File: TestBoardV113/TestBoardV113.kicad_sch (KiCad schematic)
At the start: 98 parts, among them J1 Conn_01x02_Socket, J10 Conn_01x02_Pin, J11 Conn_01x02_Pin, J12 Conn_01x02_Pin, J13 Conn_02x03_Odd_Even, J14 Conn_02x03_Odd_Even, J15 Conn_01x02_Pin, J16 Conn_02x03_Odd_Even, J17 Conn_01x01_Pin, J18 Conn_01x28_Socket, J19 Conn_01x01_Pin, J2 Conn_02x06_Odd_Even, J20 Conn_01x01_Pin, J21 Conn_01x28_Socket, J22 Conn_01x02_Pin, J23 Conn_01x02_Socket, J24 Conn_01x01_Pin, J25 Conn_01x02_Pin, J26 Conn_01x02_Pin, J27 Conn_02x03_Odd_Even, J28 Conn_01x02_Socket, J3 Conn_01x02_Pin, J4 Conn_01x02_Pin, J5 Conn_01x02_Pin, J6 Conn_01x02_Pin, J7 Conn_01x03_Pin, J8 Conn_01x03_Pin, J9 Conn_01x03_Pin, SW1 SW_DIP_x07, U1 NCP705MTADJTCG, U2 NCP705MTADJTCG, U3 NCP705MTADJTCG, U4 TAR5SxxU_SOT353F, U5 TXB0104PW, U6 TXB0104PW

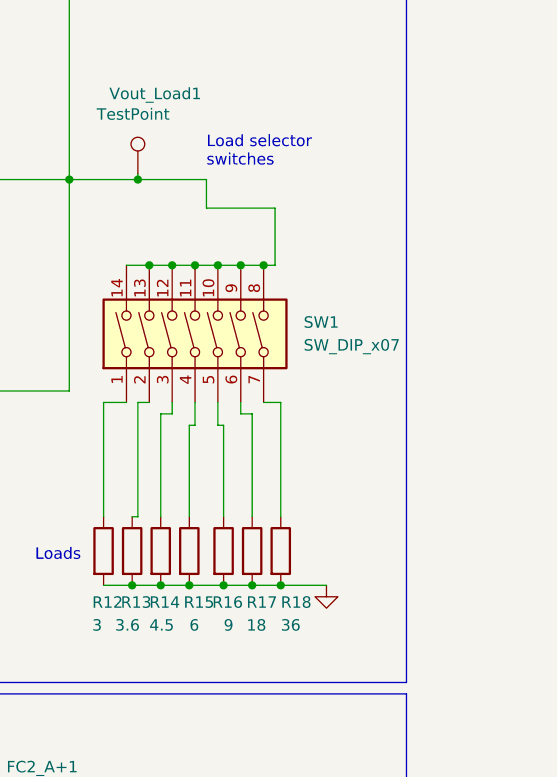
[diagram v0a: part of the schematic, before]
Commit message: added external load connector
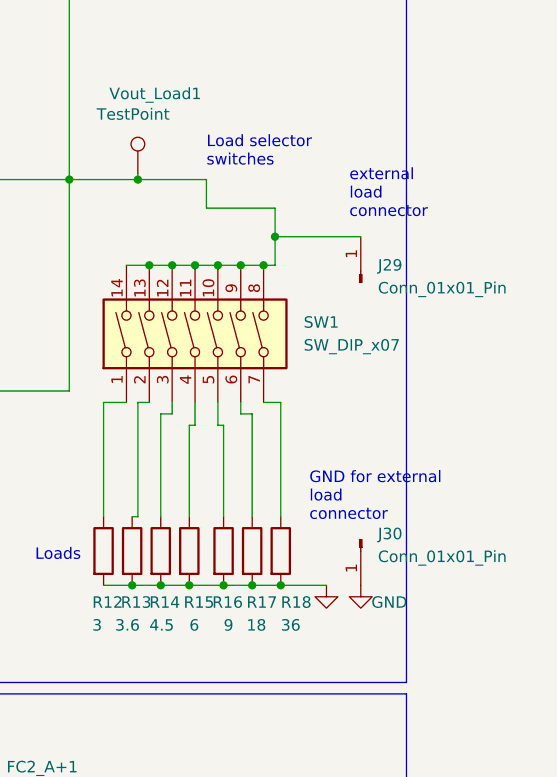
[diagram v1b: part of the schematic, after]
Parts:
- added J29, J30: Conn_01x01_Pin, Connector_PinHeader_2.54mm:PinHeader_1x01_P2.54mm_Vertical, symbol Connector:Conn_01x01_Pin
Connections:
- net GND: now also J30.1 (Pin_1)
- net Load conection +: now also J29.1 (Pin_1)
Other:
- note added: "GND for external load connector"
- note added: "external load connector"
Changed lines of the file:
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@@
   (junction (at 182.88 87.63) (diameter 0) (color 0 0 0 0)
   )
+  (junction (at 372.745 46.99) (diameter 0) (color 0 0 0 0)
+  )
   (junction (at 135.255 186.69) (diameter 0) (color 0 0 0 0)
   )
@@
     (stroke (width 0) (type default))
   )
+  (wire (pts (xy 372.745 46.99) (xy 372.745 50.165))
+    (stroke (width 0) (type default))
+  )
   (wire (pts (xy 360.045 85.725) (xy 363.22 85.725))
     (stroke (width 0) (type default))
@@
     (stroke (width 0) (type default))
   )
+  (wire (pts (xy 382.27 46.99) (xy 372.745 46.99))
+    (stroke (width 0) (type default))
+  )
   (wire (pts (xy 357.505 40.64) (xy 365.125 40.64))
     (stroke (width 0) (type default))
@@
     (stroke (width 0) (type default))
   )
-  (wire (pts (xy 372.745 43.815) (xy 372.745 50.165))
+  (wire (pts (xy 372.745 43.815) (xy 372.745 46.99))
     (stroke (width 0) (type default))
   )
@@
     (effects (font (size 1.27 1.27)) (justify left bottom))
   )
+  (text "external\nload \nconnector\n" (at 381 45.085 0)
+    (effects (font (size 1.27 1.27)) (justify left bottom))
+  )
   (text "PWM D1-D4 3V3 input " (at 107.95 217.805 90)
     (effects (font (size 1.27 1.27)) (justify left bottom))
@@
     (effects (font (size 1.27 1.27)) (justify left bottom))
   )
+  (text "GND for external\nload \nconnector\n" (at 376.555 78.74 0)
+    (effects (font (size 1.27 1.27)) (justify left bottom))
+  )
   (text "vdda1 LDO" (at 91.44 21.59 0)
     (effects (font (size 1.27 1.27)) (justify left bottom))
@@
     )
   )
+  (symbol (lib_id "Connector:Conn_01x01_Pin") (at 382.27 80.645 270) (unit 1)
+    (in_bom yes) (on_board yes) (dnp no) (fields_autoplaced)
+    (property "Reference" "J30" (at 384.175 80.01 90)
+      (effects (font (size 1.27 1.27)) (justify left))
+    )
+    (property "Value" "Conn_01x01_Pin" (at 384.175 82.55 90)
+      (effects (font (size 1.27 1.27)) (justify left))
+    )
+    (property "Footprint" "Connector_PinHeader_2.54mm:PinHeader_1x01_P2.54mm_Vertical" (at 382.27 80.645 0)
+      (effects (font (size 1.27 1.27)) hide)
+    )
+    (property "Datasheet" "~" (at 382.27 80.645 0)
+      (effects (font (size 1.27 1.27)) hide)
+    )
+    (pin "1")
+    (instances
+      (project "TestBoardV113"
+        (path "/4de6d057-85e0-4efd-8c0f-256b0c8a5cf9"
+          (reference "J30") (unit 1)
+        )
+      )
+    )
+  )
   (symbol (lib_id "Device:C") (at 120.015 67.31 0) (unit 1)
     (in_bom yes) (on_board yes) (dnp no)
@@
     )
   )
+  (symbol (lib_id "Connector:Conn_01x01_Pin") (at 382.27 52.07 90) (unit 1)
+    (in_bom yes) (on_board yes) (dnp no) (fields_autoplaced)
+    (property "Reference" "J29" (at 384.175 50.165 90)
+      (effects (font (size 1.27 1.27)) (justify right))
+    )
+    (property "Value" "Conn_01x01_Pin" (at 384.175 52.705 90)
+      (effects (font (size 1.27 1.27)) (justify right))
+    )
+    (property "Footprint" "Connector_PinHeader_2.54mm:PinHeader_1x01_P2.54mm_Vertical" (at 382.27 52.07 0)
+      (effects (font (size 1.27 1.27)) hide)
+    )
+    (property "Datasheet" "~" (at 382.27 52.07 0)
+      (effects (font (size 1.27 1.27)) hide)
+    )
+    (pin "1")
+    (instances
+      (project "TestBoardV113"
+        (path "/4de6d057-85e0-4efd-8c0f-256b0c8a5cf9"
+          (reference "J29") (unit 1)
+        )
+      )
+    )
+  )
   (symbol (lib_id "power:GND") (at 35.56 190.5 270) (mirror x) (unit 1)
     (in_bom yes) (on_board yes) (dnp no) (fields_autoplaced)
@@
         )
       )
+    )
+  )
+  (symbol (lib_id "power:GND") (at 382.27 85.725 0) (unit 1)
+    (in_bom yes) (on_board yes) (dnp no)
+    (property "Reference" "#PWR042" (at 382.27 92.075 0)
+      (effects (font (size 1.27 1.27)) hide)
+    )
+    (property "Value" "GND" (at 385.445 87.63 0)
+      (effects (font (size 1.27 1.27)))
+    )
+    (property "Footprint" "" (at 382.27 85.725 0)
+      (effects (font (size 1.27 1.27)) hide)
+    )
+    (property "Datasheet" "" (at 382.27 85.725 0)
+      (effects (font (size 1.27 1.27)) hide)
+    )
+    (pin "1")
+    (instances
+      (project "TestBoardV113"
+        (path "/4de6d057-85e0-4efd-8c0f-256b0c8a5cf9"
+          (reference "#PWR042") (unit 1)
+        )
+      )

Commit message: inductors size changed
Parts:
- L1, L2: footprint Inductor_SMD:L_0805_2012Metric -> Inductor_SMD:L_1210_3225Metric
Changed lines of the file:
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@@
       (effects (font (size 1.27 1.27)))
     )
-    (property "Footprint" "Inductor_SMD:L_0805_2012Metric" (at 283.845 40.64 0)
+    (property "Footprint" "Inductor_SMD:L_1210_3225Metric" (at 283.845 40.64 0)
       (effects (font (size 1.27 1.27)) hide)
     )
@@
       (effects (font (size 1.27 1.27)))
     )
-    (property "Footprint" "Inductor_SMD:L_0805_2012Metric" (at 286.385 57.15 0)
-      (effects (font (size 1.27 1.27)) hide)
-    )
+    (property "Footprint" "Inductor_SMD:L_1210_3225Metric" (at 286.385 57.15 0)
+      (effects (font (size 1.27 1.27)) hide)
+    )
